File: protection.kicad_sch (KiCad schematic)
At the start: 27 parts, among them J16 10x2.54mm, J18 10x2.54mm, J19 10x2.54mm, J20 10x2.54mm, J21 10x2.54mm, J22 10x2.54mm, K23 TQ2-5, U6 TXS0108EPW, U7 TXS0108EPW, U8 TXS0108EPW

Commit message: First try to fit electronic on PCB
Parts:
- added D23: 1N4148, Diode_THT:D_DO-35_SOD27_P7.62mm_Horizontal, symbol Diode:1N4148
- TP71: renamed from TP134; footprint Connector_Pin:Pin_D1.2mm_L11.3mm_W3.0mm_Flat -> Connector_Pin:Pin_D1.0mm_L10.0mm
- TP72: renamed from TP135; footprint Connector_Pin:Pin_D1.2mm_L11.3mm_W3.0mm_Flat -> Connector_Pin:Pin_D1.0mm_L10.0mm
- renumbered D37 to D19, D38 to D20, D39 to D21, D40 to D22, J22 to J10, J16 to J5, J18 to J6, J19 to J7, J20 to J8, J21 to J9, K23 to K19, NT393 to NT396, NT394 to NT397, NT395 to NT398, R45 to R27, R46 to R28
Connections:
- net GND: now also D23.2 (A)
- net at K19.1, NT398.2: now also D23.1 (K)

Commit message: backup 1 bank done
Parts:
- NT396, NT397, NT398: footprint NetTie:NetTie-2_THT_Pad1.0mm -> NetTie:NetTie-2_Front1.0mm
- TP71, TP72: footprint Connector_Pin:Pin_D1.0mm_L10.0mm -> Connector_Pin:Pin_D0.9mm_L10.0mm_W2.4mm_FlatFork
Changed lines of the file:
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@@
     (property "Reference" "NT397" (id 0) (at 81.28 165.1 0))
     (property "Value" "R_ADC1" (id 1) (at 81.28 167.64 0))
-    (property "Footprint" "NetTie:NetTie-2_THT_Pad1.0mm" (id 2) (at 81.28 166.37 0)
+    (property "Footprint" "NetTie:NetTie-2_Front1.0mm" (id 2) (at 81.28 166.37 0)
       (effects (font (size 1.27 1.27)) hide)
     )
@@
     (property "Reference" "NT396" (id 0) (at 81.28 154.94 0))
     (property "Value" "R_ADC0" (id 1) (at 81.28 157.48 0))
-    (property "Footprint" "NetTie:NetTie-2_THT_Pad1.0mm" (id 2) (at 81.28 156.21 0)
+    (property "Footprint" "NetTie:NetTie-2_Front1.0mm" (id 2) (at 81.28 156.21 0)
       (effects (font (size 1.27 1.27)) hide)
     )
@@
       (effects (font (size 1.27 1.27)) (justify left))
     )
-    (property "Footprint" "Connector_Pin:Pin_D1.0mm_L10.0mm" (id 2) (at 78.74 166.37 0)
+    (property "Footprint" "Connector_Pin:Pin_D0.9mm_L10.0mm_W2.4mm_FlatFork" (id 2) (at 78.74 166.37 0)
       (effects (font (size 1.27 1.27)) hide)
     )
@@
     (property "Reference" "NT398" (id 0) (at 81.28 177.8 0))
     (property "Value" "R_ADC" (id 1) (at 81.28 180.34 0))
-    (property "Footprint" "NetTie:NetTie-2_THT_Pad1.0mm" (id 2) (at 81.28 179.07 0)
+    (property "Footprint" "NetTie:NetTie-2_Front1.0mm" (id 2) (at 81.28 179.07 0)
       (effects (font (size 1.27 1.27)) hide)
     )
@@
       (effects (font (size 1.27 1.27)) (justify left))
     )
-    (property "Footprint" "Connector_Pin:Pin_D1.0mm_L10.0mm" (id 2) (at 78.74 176.53 0)
-      (effects (font (size 1.27 1.27)) hide)
-    )
+    (property "Footprint" "Connector_Pin:Pin_D0.9mm_L10.0mm_W2.4mm_FlatFork" (id 2) (at 78.74 176.53 0)
+      (effects (font (size 1.27 1.27)) hide)
+    )

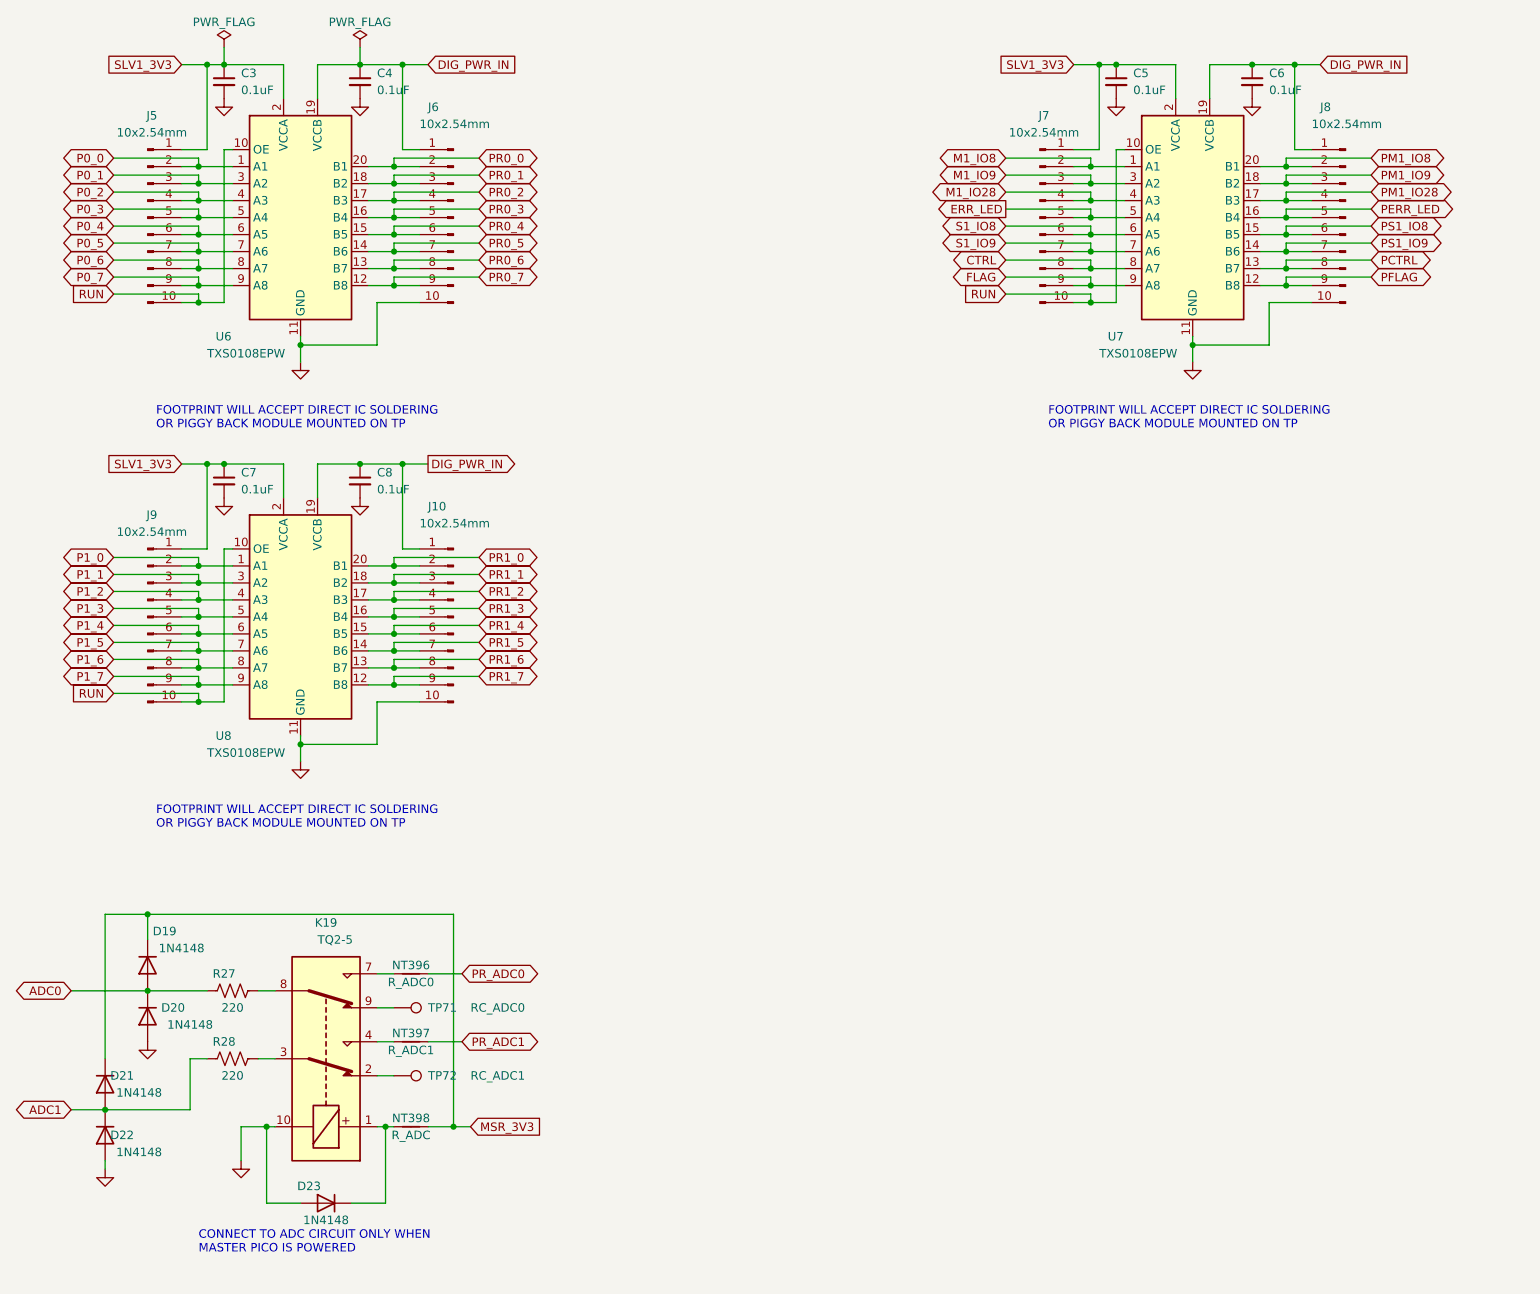
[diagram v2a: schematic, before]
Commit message: PCB Completed
PCB completed but final verification not completed
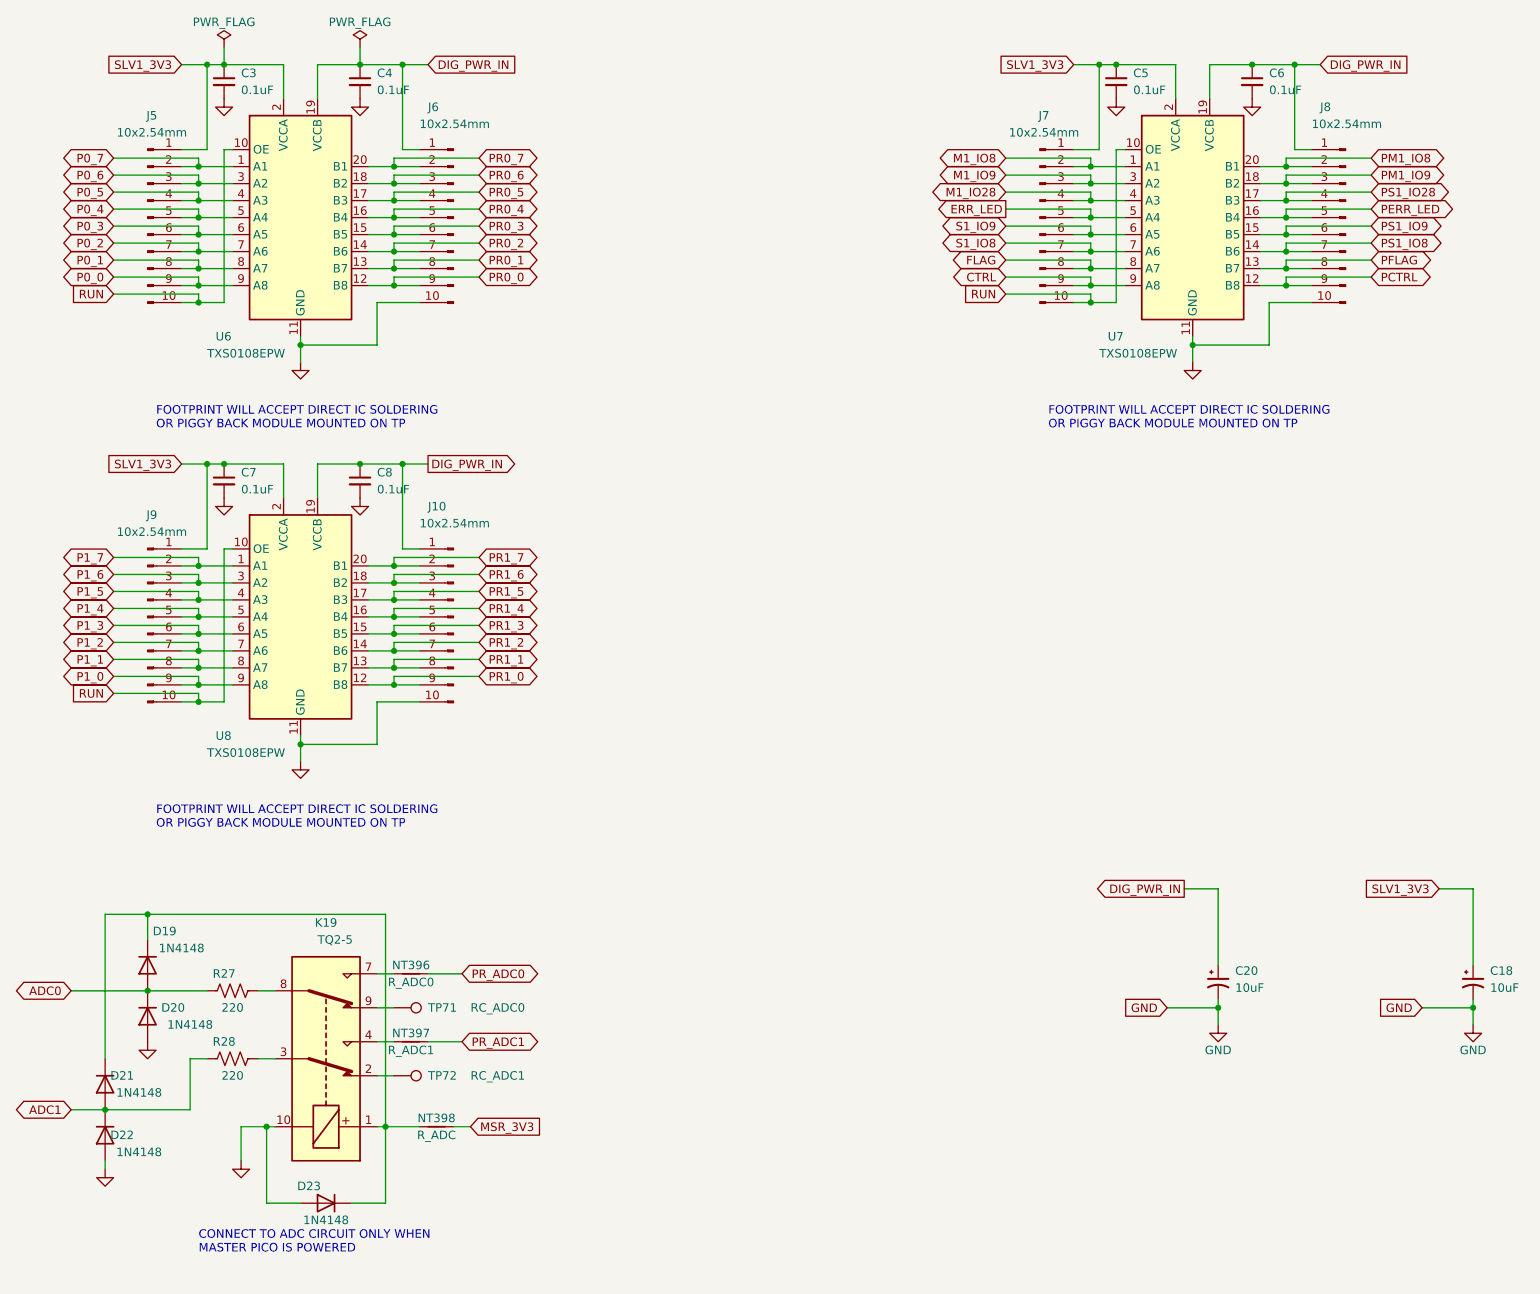
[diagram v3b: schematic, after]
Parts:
- added C18, C20: 10uF, Capacitor_THT:CP_Radial_D4.0mm_P1.50mm, symbol Device:C_Polarized_Small_US
- J10, J5, J6, J7, J8, J9: footprint Connector_PinHeader_2.54mm:PinHeader_1x10_P2.54mm_Vertical -> Connector_PinSocket_2.54mm:PinSocket_1x10_P2.54mm_Vertical
- TP71, TP72: footprint Connector_Pin:Pin_D0.9mm_L10.0mm_W2.4mm_FlatFork -> TestPoint:TestPoint_THTPad_D1.5mm_Drill0.7mm
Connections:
- net CTRL: now also J7.9 (Pin_9), U7.9 (A8); no longer J7.8 (Pin_8), U7.8 (A7)
- net DIG_PWR_IN: now also C20.1
- net FLAG: now also J7.8 (Pin_8), U7.8 (A7); no longer J7.9 (Pin_9), U7.9 (A8)
- net GND: now also C18.2, C20.2
- net MSR_3V3: no longer D19.1 (K), D21.1 (K)
- net P0_0: now also J5.9 (Pin_9), U6.9 (A8); no longer J5.2 (Pin_2), U6.1 (A1)
- net P0_1: now also J5.8 (Pin_8), U6.8 (A7); no longer J5.3 (Pin_3), U6.3 (A2)
- net P0_2: now also J5.7 (Pin_7), U6.7 (A6); no longer J5.4 (Pin_4), U6.4 (A3)
- net P0_3: now also J5.6 (Pin_6), U6.6 (A5); no longer J5.5 (Pin_5), U6.5 (A4)
- net P0_4: now also J5.5 (Pin_5), U6.5 (A4); no longer J5.6 (Pin_6), U6.6 (A5)
- net P0_5: now also J5.4 (Pin_4), U6.4 (A3); no longer J5.7 (Pin_7), U6.7 (A6)
- net P0_6: now also J5.3 (Pin_3), U6.3 (A2); no longer J5.8 (Pin_8), U6.8 (A7)
- net P0_7: now also J5.2 (Pin_2), U6.1 (A1); no longer J5.9 (Pin_9), U6.9 (A8)
- net P1_0: now also J9.9 (Pin_9), U8.9 (A8); no longer J9.2 (Pin_2), U8.1 (A1)
- net P1_1: now also J9.8 (Pin_8), U8.8 (A7); no longer J9.3 (Pin_3), U8.3 (A2)
- net P1_2: now also J9.7 (Pin_7), U8.7 (A6); no longer J9.4 (Pin_4), U8.4 (A3)
- net P1_3: now also J9.6 (Pin_6), U8.6 (A5); no longer J9.5 (Pin_5), U8.5 (A4)
- net P1_4: now also J9.5 (Pin_5), U8.5 (A4); no longer J9.6 (Pin_6), U8.6 (A5)
- net P1_5: now also J9.4 (Pin_4), U8.4 (A3); no longer J9.7 (Pin_7), U8.7 (A6)
- net P1_6: now also J9.3 (Pin_3), U8.3 (A2); no longer J9.8 (Pin_8), U8.8 (A7)
- net P1_7: now also J9.2 (Pin_2), U8.1 (A1); no longer J9.9 (Pin_9), U8.9 (A8)
- net PCTRL: now also J8.9 (Pin_9), U7.12 (B8); no longer J8.8 (Pin_8), U7.13 (B7)
- net PFLAG: now also J8.8 (Pin_8), U7.13 (B7); no longer J8.9 (Pin_9), U7.12 (B8)
- net PR0_0: now also J6.9 (Pin_9), U6.12 (B8); no longer J6.2 (Pin_2), U6.20 (B1)
- net PR0_1: now also J6.8 (Pin_8), U6.13 (B7); no longer J6.3 (Pin_3), U6.18 (B2)
- net PR0_2: now also J6.7 (Pin_7), U6.14 (B6); no longer J6.4 (Pin_4), U6.17 (B3)
- net PR0_3: now also J6.6 (Pin_6), U6.15 (B5); no longer J6.5 (Pin_5), U6.16 (B4)
- net PR0_4: now also J6.5 (Pin_5), U6.16 (B4); no longer J6.6 (Pin_6), U6.15 (B5)
- net PR0_5: now also J6.4 (Pin_4), U6.17 (B3); no longer J6.7 (Pin_7), U6.14 (B6)
- net PR0_6: now also J6.3 (Pin_3), U6.18 (B2); no longer J6.8 (Pin_8), U6.13 (B7)
- net PR0_7: now also J6.2 (Pin_2), U6.20 (B1); no longer J6.9 (Pin_9), U6.12 (B8)
- net PR1_0: now also J10.9 (Pin_9), U8.12 (B8); no longer J10.2 (Pin_2), U8.20 (B1)
- net PR1_1: now also J10.8 (Pin_8), U8.13 (B7); no longer J10.3 (Pin_3), U8.18 (B2)
- net PR1_2: now also J10.7 (Pin_7), U8.14 (B6); no longer J10.4 (Pin_4), U8.17 (B3)
- net PR1_3: now also J10.6 (Pin_6), U8.15 (B5); no longer J10.5 (Pin_5), U8.16 (B4)
- net PR1_4: now also J10.5 (Pin_5), U8.16 (B4); no longer J10.6 (Pin_6), U8.15 (B5)
- net PR1_5: now also J10.4 (Pin_4), U8.17 (B3); no longer J10.7 (Pin_7), U8.14 (B6)
- net PR1_6: now also J10.3 (Pin_3), U8.18 (B2); no longer J10.8 (Pin_8), U8.13 (B7)
- net PR1_7: now also J10.2 (Pin_2), U8.20 (B1); no longer J10.9 (Pin_9), U8.12 (B8)
- net PS1_IO8: now also J8.7 (Pin_7), U7.14 (B6); no longer J8.6 (Pin_6), U7.15 (B5)
- net PS1_IO9: now also J8.6 (Pin_6), U7.15 (B5); no longer J8.7 (Pin_7), U7.14 (B6)
- net S1_IO8: now also J7.7 (Pin_7), U7.7 (A6); no longer J7.6 (Pin_6), U7.6 (A5)
- net S1_IO9: now also J7.6 (Pin_6), U7.6 (A5); no longer J7.7 (Pin_7), U7.7 (A6)
- net SLV1_3V3: now also C18.1
- net at D23.1 (K), K19.1, NT398.2: now also D19.1 (K), D21.1 (K)
- net PM1_IO28 renamed PS1_IO28
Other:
- moved on the sheet: NT398

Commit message: update
Correction of small error
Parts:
- added Q3: 2N2222, Package_TO_SOT_THT:TO-92_Inline, symbol Transistor_BJT:2N3904
- added R5: 10K, Resistor_THT:R_Axial_DIN0207_L6.3mm_D2.5mm_P10.16mm_Horizontal, symbol Device:R_US
- added TP21: SPARE, TestPoint:TestPoint_THTPad_D1.5mm_Drill0.7mm, symbol Connector:TestPoint
- R27, R28: footprint Resistor_THT:R_Axial_DIN0309_L9.0mm_D3.2mm_P12.70mm_Horizontal -> Resistor_THT:R_Axial_DIN0207_L6.3mm_D2.5mm_P10.16mm_Horizontal
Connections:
- net GND: now also Q3.1 (E); no longer D23.2 (A), K19.10
- net MSR_3V3: now also D19.1 (K), D21.1 (K); no longer NT398.1
- net M1_IO28: no longer names the net of J7.4 (Pin_4), U7.4 (A3)
- net M1_IO28: now also TP21.1
- net PS1_IO28 renamed DIG_SPARE
- net RUN renamed OE
- net OE: now also R5.2
- new net: D23.2 (A), K19.10, NT398.1
- new net: Q3.2 (B), R5.1
- new net: NT398.2, Q3.3 (C)
- new net VCC: D23.1 (K), K19.1
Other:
- note added: "TO PROTECT PICO FOR BEING POWERED BY UUT"
- note removed: "CONNECT TO ADC CIRCUIT ONLY WHEN MASTER PICO IS POWERED"
- moved on the sheet: D19, D20, D21, D22, D23, K19, NT396, NT397, R27, R28, TP71, TP72
